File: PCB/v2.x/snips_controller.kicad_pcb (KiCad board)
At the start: 4 copper layers, 30 x 70 mm, 92 parts

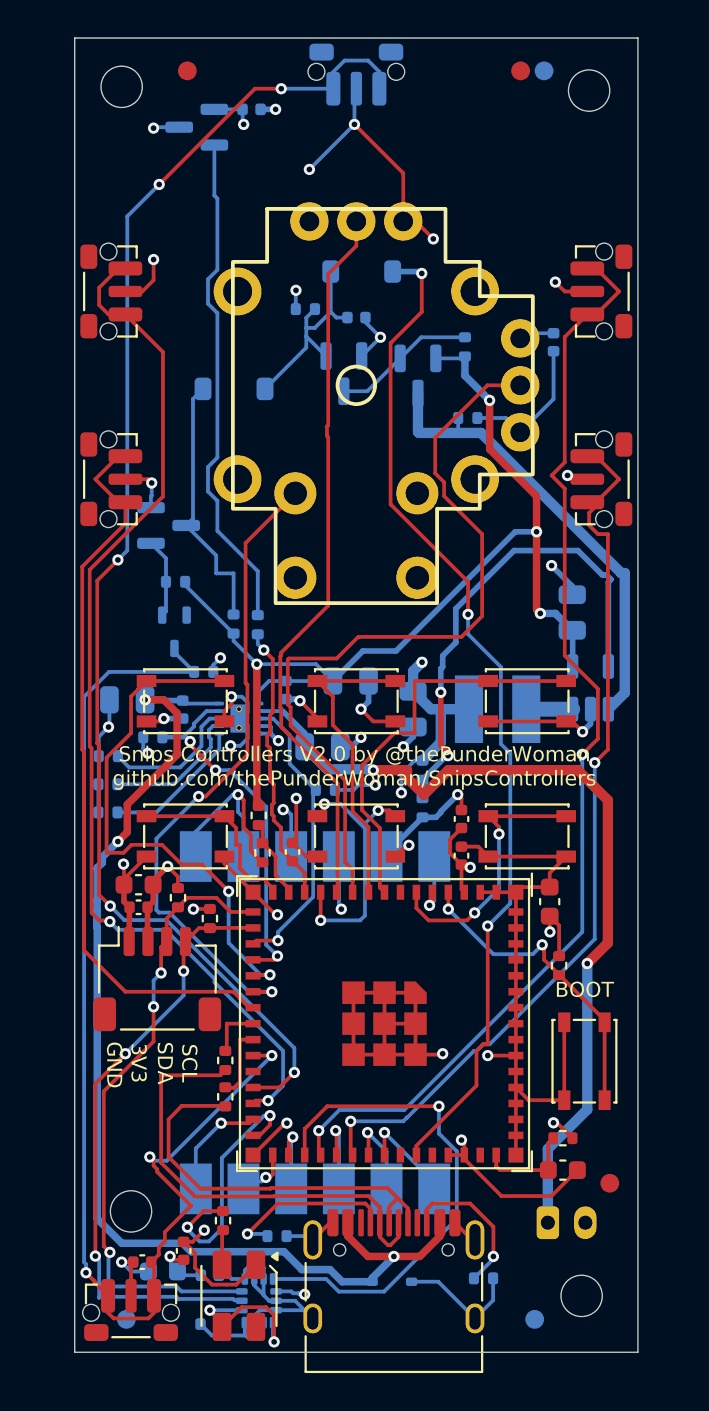
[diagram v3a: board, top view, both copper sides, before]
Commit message: V2 PCB: move PWR_HOLD to IO42 and apply review fixes (#100)
Swap PWR_HOLD and XBEE_RESET so the hold line sits on IO42, which has no
reset pull. RXD0's pull-up could re-latch the board as the rail collapses
at power-off. C_LATCH_G1 becomes 1 uF to ride through a short reset, and
firmware holds the pin with gpio_hold_en for USB uploads.

R_INV_BASE1 and R_INV_PU1 become 220k to cut the off drain. Add C_VSYS1,
move the buck input cap and feedback divider beside the IC, double the
power vias and add module GND stitching.

Rename C_3V3_* to C_MCU_* and give every BOM line its full part detail,
because PCBWay read "3V3" in the designators as a voltage rating.

Add latch_v2_sim.py and regenerate the production files.

Co-authored-by: Claude Opus 5.5 <noreply@anthropic.com>
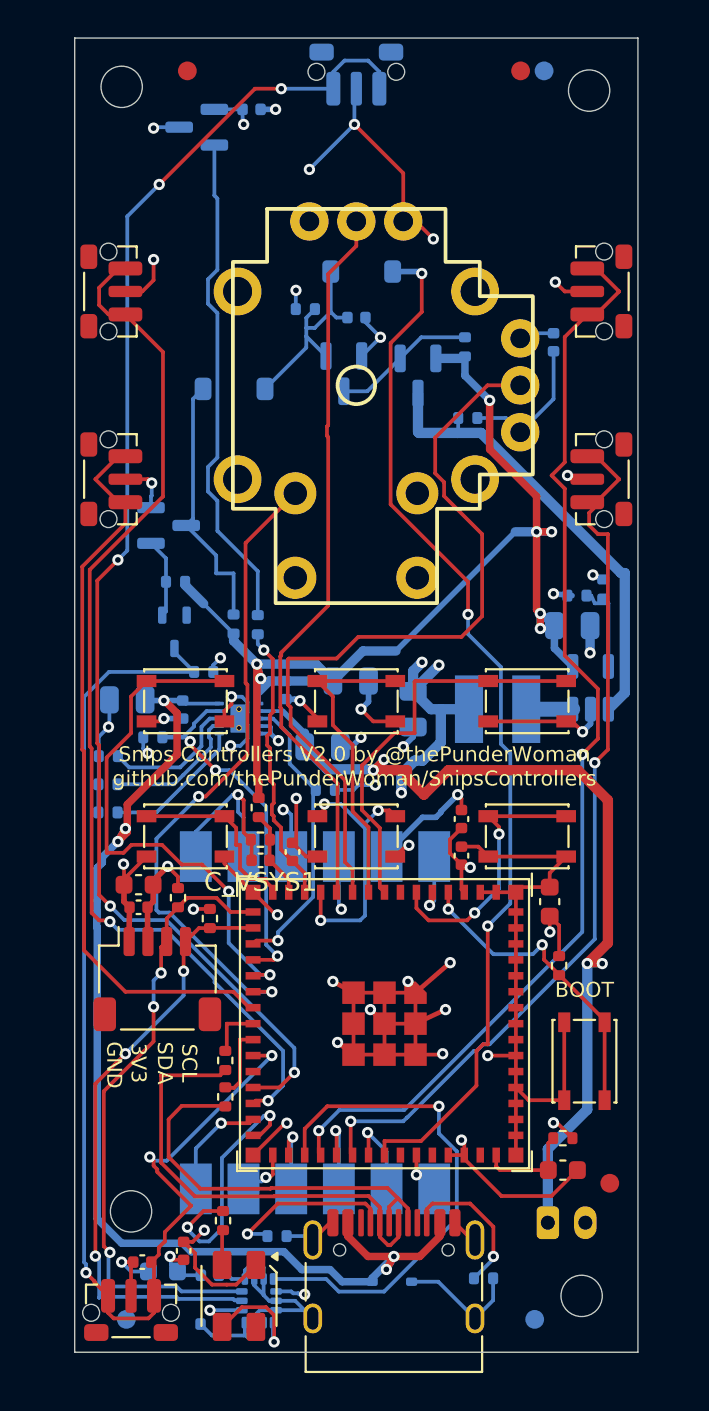
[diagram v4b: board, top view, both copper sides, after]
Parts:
- removed C_3V3_1: 10µF, Capacitor_SMD:C_0603_1608Metric
- removed C_3V3_2: 100nF, Capacitor_SMD:C_0402_1005Metric
- removed C_3V3_3: 39pF, C_0402_1005Metric
- added C_MCU_1: 10µF 10V X5R ±10% | CL10A106KP8NNNC | Samsung | 0603, C_0603_1608Metric, F.Cu at (145.3, 106.0)
- added C_MCU_2: 100nF 16V X7R ±10% | CL05B104KO5NNNC | Samsung | 0402, C_0402_1005Metric, F.Cu at (140.6, 101.6)
- added C_MCU_3: 39pF 50V NP0 ±5% | CC0402JRNPO9BN390 | Yageo | 0402, C_0402_1005Metric, F.Cu at (140.6, 103.5)
- added C_VSYS1: 100nF 16V X7R ±10% | CL05B104KO5NNNC | Samsung | 0402, C_0402_1005Metric, F.Cu at (129.9, 103.8)
- BT1: value PH 2-pin battery RIGHT-ANGLE HORIZONTAL -> JST PH 2-pin 2mm | S2B-PH-K(LF)(SN) | JST | Through-hole | RIGHT-ANGLE HORIZONTAL not vertical
- C_BAT1, C_BUCK_IN1, C_SYS_1, C_VIN_1: value 10µF -> 10µF 25V X5R ±10% | CL21A106KAYNNNE | Samsung | 0805
- C_BUCK_OUT1: value 22µF -> 22µF 25V X5R ±20% | CL21A226MAQNNNE | Samsung | 0805
- C_DBNC1, C_HALL1, C_IMU_1, C_OLED_2, C_RGB1, C_STICK1, C_SYS_2, C_TRIG1, C_VIN_2: value 100nF -> 100nF 16V X7R ±10% | CL05B104KO5NNNC | Samsung | 0402
- C_EN1, C_OLED_1: value 1µF -> 1µF 50V X5R ±10% | CL10A105KB8NNNC | Samsung | 0603
- C_IMU_2: value 2.2µF -> 2.2µF 10V X7R ±10% | CL10B225KP8NNNC | Samsung | 0603
- C_IMU_3: value 10nF -> 10nF 50V X7R ±10% | CL05B103KB5NNNC | Samsung | 0402
- C_LATCH_G1: value 100nF -> 1µF 6.3V X5R ±10% | CL05A105KQ5NNNC | Samsung | 0402
- D_INV_ISO1: value BAT54W-7-F -> Schottky diode 30V 200mA | BAT54W-7-F | Diodes Inc | SOT-323
- D_OR1, D_OR2: value 1N4148W -> 1N4148W switching diode 75V 150mA | 1N4148W | ST | SOD-123
- D_RGB1: value SK6812MINI-HS-012 -> Addressable RGB LED | SK6812MINI-HS | OPSCO | 3.5x3.5mm SMD | top-mount lens up
- D_VBUS_TVS1: value TPPESD5V0S1BA -> TVS diode 5V bidirectional | TPPESD5V0S1BA | TECH PUBLIC | SOD-323
- J_STICK1: value GuliKit_Thumbstick -> Hall thumbstick | GuliKit_Thumbstick | GuliKit | Through-hole | DNP - hand-fitted - do not assemble
- J_USB1: value USB-C -> USB-C receptacle 16-pin | TYPE-C-31-M-12 | Hroparts Elec | SMD with through-hole shell tabs | right-angle
- L_BUCK1: value 2.2µH -> 2.2µH ±20% 2.9A 44mΩ power inductor | SRN4018-2R2M | Bourns | SMD 4x4mm
- Q_INV1: value MMBT3904(RANGE:100-300) -> NPN transistor 40V 200mA hFE 100-300 | MMBT3904(RANGE:100-300) | JCET | SOT-23
- Q_LATCH1: value AO3400A -> N-channel MOSFET 30V 5.7A | AO3400A | AOS | SOT-23
- Q_PWR1: value AO3401A -> P-channel MOSFET 30V 4A | AO3401A | AOS | SOT-23
- R_BOOT_PU1, R_EN_PU1, R_STAT1, R_STAT2, R_TS1: value 10kΩ -> 10kΩ ±1% 62.5mW | 0402WGF1002TCE | UNI-ROYAL | 0402
- R_BTN_PU1, R_GATE1, R_PWR_EN_PD1, R_VSYS2: value 100kΩ -> 100kΩ ±1% 62.5mW | 0402WGF1003TCE | UNI-ROYAL | 0402
- R_CC1, R_CC2: value 5.1kΩ -> 5.1kΩ ±1% 62.5mW | 0402WGF5101TCE | UNI-ROYAL | 0402
- R_FB1: value 255kΩ -> 255kΩ ±1% 62.5mW | RC0402FR-07255KL | Yageo | 0402
- R_FB2: value 56.2kΩ -> 56.2kΩ ±1% 62.5mW | RC0402FR-0756K2L | Yageo | 0402
- R_I2C_SCL1, R_I2C_SDA1: value 4.7kΩ -> 4.7kΩ ±1% 62.5mW | 0402WGF4701TCE | UNI-ROYAL | 0402
- R_INV_BASE1, R_INV_PU1: value 100kΩ -> 220kΩ ±1% 62.5mW | 0402WGF2203TCE | UNI-ROYAL | 0402
- R_ISET1: value 604Ω -> 604Ω ±1% 62.5mW | AC0402FR-07604RL | Yageo | 0402
- R_LATCH_G1: value 1MΩ -> 1MΩ ±1% 62.5mW | 0402WGF1004TCE | UNI-ROYAL | 0402
- R_RGB1: value 470Ω -> 470Ω ±1% 62.5mW | 0402WGF4700TCE | UNI-ROYAL | 0402
- R_TRIG1: value 1kΩ -> 1kΩ ±1% 62.5mW | 0402WGF1001TCE | UNI-ROYAL | 0402
- R_USB_DM1, R_USB_DP1: value 27Ω -> 27Ω ±1% 62.5mW | RC0402FR-0727RL | Yageo | 0402
- R_VSET1: value 18kΩ -> 18kΩ ±1% 62.5mW | RC0402FR-0718KL | Yageo | 0402
- R_VSYS1: value 200kΩ -> 200kΩ ±1% 62.5mW | 0402WGF2003TCE | UNI-ROYAL | 0402
- SW_BOOT1, SW_MACRO1, SW_MACRO2, SW_MACRO3, SW_MACRO4, SW_MACRO5, SW_MACRO6: value SKRPABE010 -> Tact switch 1.6N 100k cycles | SKRPABE010 | Alps | SMD 4.2x3.2x2.5mm | top actuated
- SW_PWR1, SW_THR_DN1, SW_THR_UP1, SW_TRIG_DIG1, SW_VOL_DN1, SW_VOL_UP1: value SKRTLAE010 -> Side-push tact switch 1.6N 100k cycles | SKRTLAE010 | Alps | SMD 4.5x3.4x3.3mm | right-angle
- U_BUCK1: value TLV62569DBVR -> Adjustable buck converter 2A | TLV62569DBVR | TI | SOT-23-5
- U_CHG1: value BQ25185DLHR -> 1-cell Li-ion charger 1A | BQ25185DLHR | TI | WSON-10
- U_HALL1: value DRV5055A2QDBZR -> Linear hall sensor A2 ±42mT | DRV5055A2QDBZR | TI | SOT-23
- U_IMU1: value ICM-42670-P -> 6-axis IMU | ICM-42670-P | TDK InvenSense | LGA-14 2.5x3mm
- U_MCU1: value ESP32-S3-MINI-1U-N8 -> Wi-Fi BLE module 8MB flash no PSRAM | ESP32-S3-MINI-1U-N8 | Espressif | SMD module 15.4x15.4mm | N8 variant with extern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
- U_OLED1: value Qwiic connector -> JST SH 4-pin 1mm Qwiic | SM04B-SRSS-TB(LF)(SN) | JST | SMD | side entry right-angle
- U_XBEE1: value XBee carrier -> XBee carrier pads no part | Snips XBee carrier | Snips Controllers | Copper pads only | DNP - hand-soldered daughter bo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
- moved R_FB2 15.1 mm to (148.2, 89.3), turned to 90 degrees
- moved R_FB1 12.4 mm to (146.8, 89.7), turned to 180 degrees
- moved R_VSYS2 0.71 mm to (129.9, 102.7), turned to 180 degrees
- moved C_BUCK_IN1 0.70 mm to (146.5, 91.3), turned to 0 degrees
- moved R_VSYS1 0.42 mm to (129.8, 101.0)
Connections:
- U_MCU1 pad 38: /XBee/XBEE_RESET -> /MCU_Core/PWR_HOLD
- U_MCU1 pad 40: /MCU_Core/PWR_HOLD -> /XBee/XBEE_RESET
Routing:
- net /Power_Buck/BUCK_FB: track 26.1 -> 5.16 mm, vias 2 -> 0
- net GND: track 208.0 -> 215.7 mm, vias 34 -> 41
- net VSYS: track 57.9 -> 61.7 mm, vias 4 -> 7
- net VBAT: track 46.1 -> 49.3 mm, vias 2 -> 4
- net 3V3: track 53.7 -> 56.7 mm, vias 17 -> 19
- net /XBee/XBEE_RESET: track 5.30 -> 2.75 mm
- net VBUS: track 59.8 -> 62.1 mm, vias 3 -> 5
- net /MCU_Core/PWR_HOLD: track 54.1 -> 55.9 mm

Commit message: V2 PCB: move PWR_HOLD to IO3 so it holds through USB uploads
A bench test on V1 hardware showed that IO42's digital-pad hold does not
survive the USB reset that ends every upload, so the board would lose
power mid-upload. IO3 is an RTC pad, and its hold lasted through a full
upload with the pin still high.

IO3 has no reset pull, so the power-off protection stays, its strap is
ignored at default eFuses, and its power-up glitch is low only, which
D_OR2 blocks. XBEE_RESET stays on RXD0. The route to pad 7 is shorter and
adds no vias. Regenerate the production files.

Co-Authored-By: Claude Opus 5.5 <noreply@anthropic.com>
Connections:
- U_MCU1 pad 38: /MCU_Core/PWR_HOLD -> (no net)
- U_MCU1 pad 7: (no net) -> /MCU_Core/PWR_HOLD
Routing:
- net /MCU_Core/PWR_HOLD: track 55.9 -> 46.0 mm
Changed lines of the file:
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@@
 			)
 		)
-		(property "Stackup Source" "PCB/v2.x/stackup/board.kdl:107"
+		(property "Stackup Source" "PCB/v2.x/stackup/board.kdl:108"
 			(at 0 2 90)
 			(layer "F.SilkS")
@@
 			)
 		)
-		(property "Stackup Source" "PCB/v2.x/stackup/board.kdl:110"
+		(property "Stackup Source" "PCB/v2.x/stackup/board.kdl:111"
 			(at 0 2 0)
 			(layer "F.SilkS")
@@
 			)
 		)
-		(property "Stackup Source" "PCB/v2.x/stackup/board.kdl:99"
+		(property "Stackup Source" "PCB/v2.x/stackup/board.kdl:100"
 			(at 0 -2 90)
 			(layer "F.SilkS")
@@
 			(size 0.4 0.8)
 			(layers "F.Cu" "F.Mask" "F.Paste")
+			(net "/MCU_Core/PWR_HOLD")
 		)
 		(pad "8" smd rect
@@
 			(size 0.4 0.8)
 			(layers "F.Cu" "F.Mask" "F.Paste")
-			(net "/MCU_Core/PWR_HOLD")
 		)
 		(pad "39" smd rect
@@
 			)
 		)
-		(property "Stackup Source" "PCB/v2.x/stackup/board.kdl:104"
+		(property "Stackup Source" "PCB/v2.x/stackup/board.kdl:105"
 			(at 0 2 90)
 			(layer "F.SilkS")
@@
 			)
 		)
-		(property "Stackup Source" "PCB/v2.x/stackup/board.kdl:103"
+		(property "Stackup Source" "PCB/v2.x/stackup/board.kdl:104"
 			(at 0 2 90)
 			(layer "F.SilkS")
@@
 			)
 		)
-		(property "Stackup Source" "PCB/v2.x/stackup/board.kdl:109"
+		(property "Stackup Source" "PCB/v2.x/stackup/board.kdl:110"
 			(at 0 -2 90)
 			(layer "B.SilkS")
@@
 			)
 		)
-		(property "Stackup Source" "PCB/v2.x/stackup/board.kdl:102"
+		(property "Stackup Source" "PCB/v2.x/stackup/board.kdl:103"
 			(at 0 -2 180)
 			(layer "B.SilkS")
@@
 			)
 		)
-		(property "Stackup Source" "PCB/v2.x/stackup/board.kdl:108"
+		(property "Stackup Source" "PCB/v2.x/stackup/board.kdl:109"
 			(at 0 -2 180)
 			(layer "B.SilkS")
@@
 			)
 		)
-		(property "Stackup Source" "PCB/v2.x/stackup/board.kdl:106"
+		(property "Stackup Source" "PCB/v2.x/stackup/board.kdl:107"
 			(at 0 -2 270)
 			(layer "B.SilkS")
@@
 	)
 	(segment
+		(start 138.485 74.588529)
+		(end 138.485 72.539999)
+		(width 0.2)
+		(layer "F.Cu")
+		(net "/MCU_Core/PWR_HOLD")
+	)
+	(segment
+		(start 136.825 76.248529)
+		(end 138.485 74.588529)
+		(width 0.2)
+		(layer "F.Cu")
+		(net "/MCU_Core/PWR_HOLD")
+	)
+	(segment
+		(start 137.65 106.4)
+		(end 138.65 107.4)
+		(width 0.2)
+		(layer "F.Cu")
+		(net "/MCU_Core/PWR_HOLD")
+	)
+	(segment
+		(start 137.65 105.8)
+		(end 137.65 106.4)
+		(width 0.2)
+		(layer "F.Cu")
+		(net "/MCU_Core/PWR_HOLD")
+	)
+	(segment
+		(start 136.825 84.840255)
+		(end 136.825 76.248529)
+		(width 0.2)
+		(layer "F.Cu")
+		(net "/MCU_Core/PWR_HOLD")
+	)
+	(segment
+		(start 137.35 105.5)
+		(end 137.65 105.8)
+		(width 0.2)
+		(layer "F.Cu")
+		(net "/MCU_Core/PWR_HOLD")
+	)
+	(segment
+		(start 141.9 107.4)
+		(end 142 107.3)
+		(width 0.2)
+		(layer "F.Cu")
+		(net "/MCU_Core/PWR_HOLD")
+	)
+	(segment
+		(start 140.95 88.965255)
+		(end 136.825 84.840255)
+		(width 0.2)
+		(layer "F.Cu")
+		(net "/MCU_Core/PWR_HOLD")
+	)
+	(segment
+		(start 140.95 90.7)
+		(end 140.95 88.965255)
+		(width 0.2)
+		(layer "F.Cu")
+		(net "/MCU_Core/PWR_HOLD")
+	)
+	(segment
+		(start 138.65 107.4)
+		(end 141.9 107.4)
+		(width 0.2)
+		(layer "F.Cu")
+		(net "/MCU_Core/PWR_HOLD")
+	)
+	(via
+		(at 140.95 90.7)
+		(size 0.6)
+		(drill 0.3)
+		(layers "F.Cu" "B.Cu")
+		(net "/MCU_Core/PWR_HOLD")
+	)
+	(via
+		(at 138.485 72.539999)
+		(size 0.6)
+		(drill 0.3)
+		(layers "F.Cu" "B.Cu")
+		(net "/MCU_Core/PWR_HOLD")
+	)
+	(via
+		(at 142 107.3)
+		(size 0.6)
+		(drill 0.3)
+		(layers "F.Cu" "B.Cu")
+		(net "/MCU_Core/PWR_HOLD")
+	)
+	(segment
+		(start 142.7 97.6)
+		(end 142.7 93.5)
+		(width 0.2)
+		(layer "B.Cu")
+		(net "/MCU_Core/PWR_HOLD")
+	)
+	(segment
+		(start 143.2 98.1)
+		(end 142.7 97.6)
+		(width 0.2)
+		(layer "B.Cu")
+		(net "/MCU_Core/PWR_HOLD")
+	)
+	(segment
+		(start 142 107.3)
+		(end 143.2 106.1)
+		(width 0.2)
+		(layer "B.Cu")
+		(net "/MCU_Core/PWR_HOLD")
+	)
+	(segment
+		(start 138.385 72.44)
+		(end 138.485 72.539999)
+		(width 0.3)
+		(layer "B.Cu")
+		(net "/MCU_Core/PWR_HOLD")
+	)
+	(segment
+		(start 143.2 106.1)
+		(end 143.2 98.1)
+		(width 0.2)
+		(layer "B.Cu")
+		(net "/MCU_Core/PWR_HOLD")
+	)
+	(segment
+		(start 136.935 72.44)
+		(end 138.385 72.44)
+		(width 0.3)
+		(layer "B.Cu")
+		(net "/MCU_Core/PWR_HOLD")
+	)
+	(segment
+		(start 140.95 91.75)
+		(end 140.95 90.7)
+		(width 0.2)
+		(layer "B.Cu")
+		(net "/MCU_Core/PWR_HOLD")
+	)
+	(segment
+		(start 142.7 93.5)
+		(end 140.95 91.75)
+		(width 0.2)
+		(layer "B.Cu")
+		(net "/MCU_Core/PWR_HOLD")
+	)
+	(segment
 		(start 131.4 93.051471)
 		(end 133.948529 93.051471)
@@
 	)
 	(segment
-		(start 138.485 74.588529)
-		(end 138.485 72.539999)
-		(width 0.2)
-		(layer "F.Cu")
-		(net "/MCU_Core/PWR_HOLD")
-	)
-	(segment
-		(start 141.4 113.951471)
-		(end 141.751471 113.6)
-		(width 0.2)
-		(layer "F.Cu")
-		(net "/MCU_Core/PWR_HOLD")
-	)
-	(segment
-		(start 136.825 76.248529)
-		(end 138.485 74.588529)
-		(width 0.2)
-		(layer "F.Cu")
-		(net "/MCU_Core/PWR_HOLD")
-	)
-	(segment
-		(start 136.5 119.5)
-		(end 136.5 118.75)
-		(width 0.2)
-		(layer "F.Cu")
-		(net "/MCU_Core/PWR_HOLD")
-	)
-	(segment
-		(start 138.45 118.75)
-		(end 141.4 115.8)
-		(width 0.2)
-		(layer "F.Cu")
-		(net "/MCU_Core/PWR_HOLD")
-	)
-	(segment
-		(start 136.825 84.840255)
-		(end 136.825 76.248529)
-		(width 0.2)
-		(layer "F.Cu")
-		(net "/MCU_Core/PWR_HOLD")
-	)
-	(segment
-		(start 140.95 88.965255)
-		(end 136.825 84.840255)
-		(width 0.2)
-		(layer "F.Cu")
-		(net "/MCU_Core/PWR_HOLD")
-	)
-	(segment
-		(start 140.95 90.7)
-		(end 140.95 88.965255)
-		(width 0.2)
-		(layer "F.Cu")
-		(net "/MCU_Core/PWR_HOLD")
-	)
-	(segment
-		(start 142 113.6)
-		(end 142 107.3)
-		(width 0.2)
-		(layer "F.Cu")
-		(net "/MCU_Core/PWR_HOLD")
-	)
-	(segment
-		(start 141.4 115.8)
-		(end 141.4 113.951471)
-		(width 0.2)
-		(layer "F.Cu")
-		(net "/MCU_Core/PWR_HOLD")
-	)
-	(segment
-		(start 141.751471 113.6)
-		(end 142 113.6)
-		(width 0.2)
-		(layer "F.Cu")
-		(net "/MCU_Core/PWR_HOLD")
-	)
-	(segment
-		(start 136.5 118.75)
-		(end 138.45 118.75)
-		(width 0.2)
-		(layer "F.Cu")
-		(net "/MCU_Core/PWR_HOLD")
-	)
-	(via
-		(at 140.95 90.7)
-		(size 0.6)
-		(drill 0.3)
-		(layers "F.Cu" "B.Cu")
-		(net "/MCU_Core/PWR_HOLD")
-	)
-	(via
-		(at 138.485 72.539999)
-		(size 0.6)
-		(drill 0.3)
-		(layers "F.Cu" "B.Cu")
-		(net "/MCU_Core/PWR_HOLD")
-	)
-	(via
-		(at 142 107.3)
-		(size 0.6)
-		(drill 0.3)
-		(layers "F.Cu" "B.Cu")
-		(net "/MCU_Core/PWR_HOLD")
-	)
-	(segment
-		(start 142.7 97.6)
-		(end 142.7 93.5)
-		(width 0.2)
-		(layer "B.Cu")
-		(net "/MCU_Core/PWR_HOLD")
-	)
-	(segment
-		(start 143.2 98.1)
-		(end 142.7 97.6)
-		(width 0.2)
-		(layer "B.Cu")
-		(net "/MCU_Core/PWR_HOLD")
-	)
-	(segment
-		(start 142 107.3)
-		(end 143.2 106.1)
-		(width 0.2)
-		(layer "B.Cu")
-		(net "/MCU_Core/PWR_HOLD")
-	)
-	(segment
-		(start 138.385 72.44)
-		(end 138.485 72.539999)
-		(width 0.3)
-		(layer "B.Cu")
-		(net "/MCU_Core/PWR_HOLD")
-	)
-	(segment
-		(start 143.2 106.1)
-		(end 143.2 98.1)
-		(width 0.2)
-		(layer "B.Cu")
-		(net "/MCU_Core/PWR_HOLD")
-	)
-	(segment
-		(start 136.935 72.44)
-		(end 138.385 72.44)
-		(width 0.3)
-		(layer "B.Cu")
-		(net "/MCU_Core/PWR_HOLD")
-	)
-	(segment
-		(start 140.95 91.75)
-		(end 140.95 90.7)
-		(width 0.2)
-		(layer "B.Cu")
-		(net "/MCU_Core/PWR_HOLD")
-	)
-	(segment
-		(start 142.7 93.5)
-		(end 140.95 91.75)
-		(width 0.2)
-		(layer "B.Cu")
-		(net "/MCU_Core/PWR_HOLD")
-	)
-	(segment

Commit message: V2 PCB: give the power latch hysteresis and hold it from RXD0
IO3's gpio_hold survived a USB upload on V1 hardware, but it leaves the
latch depending on firmware, and it was only tested with no load. Move
PWR_HOLD back to RXD0, whose pull-up holds the latch through any reset or
upload with no firmware help, and put XBEE_RESET on IO42. IO3 goes back
to unconnected.

That pull-up returns as the rail collapses at power-off, with the gate
sitting at threshold, so the latch needs hysteresis. C_LATCH_FB1 (470 nF,
PWR_EN to gate) kicks the gate clear as PWR_EN falls. It also couples a
rising gate back into PWR_EN, which restarts the board at the capacitor
tolerance extremes with a 100k pull-down, so R_PWR_EN_PD1 is now 22k.

Rewrite latch_v2_sim.py around this behaviour, with 47 checks, and
regenerate the production files.

Co-Authored-By: Claude Opus 5.5 <noreply@anthropic.com>
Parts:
- added C_LATCH_FB1: 470nF 25V X7R ±10% | CL10B474KA8NNNC | Samsung | 0603, C_0603_1608Metric, B.Cu at (137.4, 80.8)
- R_PWR_EN_PD1: value 100kΩ ±1% 62.5mW | 0402WGF1003TCE | UNI-ROYAL | 0402 -> 22kΩ ±1% 62.5mW | 0402WGF2202TCE | UNI-ROYAL | 0402
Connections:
- U_MCU1 pad 38: (no net) -> /XBee/XBEE_RESET
- U_MCU1 pad 40: /XBee/XBEE_RESET -> /MCU_Core/PWR_HOLD
- U_MCU1 pad 7: /MCU_Core/PWR_HOLD -> (no net)
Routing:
- net /MCU_Core/PWR_HOLD: track 46.0 -> 54.1 mm
- net /Power_Control/PWR_LATCH_G: track 11.7 -> 18.0 mm
- net /XBee/XBEE_RESET: track 2.75 -> 4.13 mm
